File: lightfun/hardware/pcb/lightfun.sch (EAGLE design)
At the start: 10 parts, among them J1 FIRMWARE, P1 ESP8266, P2 ESP8266 CONNECTOR, P3 +5V GND, P4 TX RX, P5 GND, P6 +5V GND IO0 IO2, T1 LM2937ET

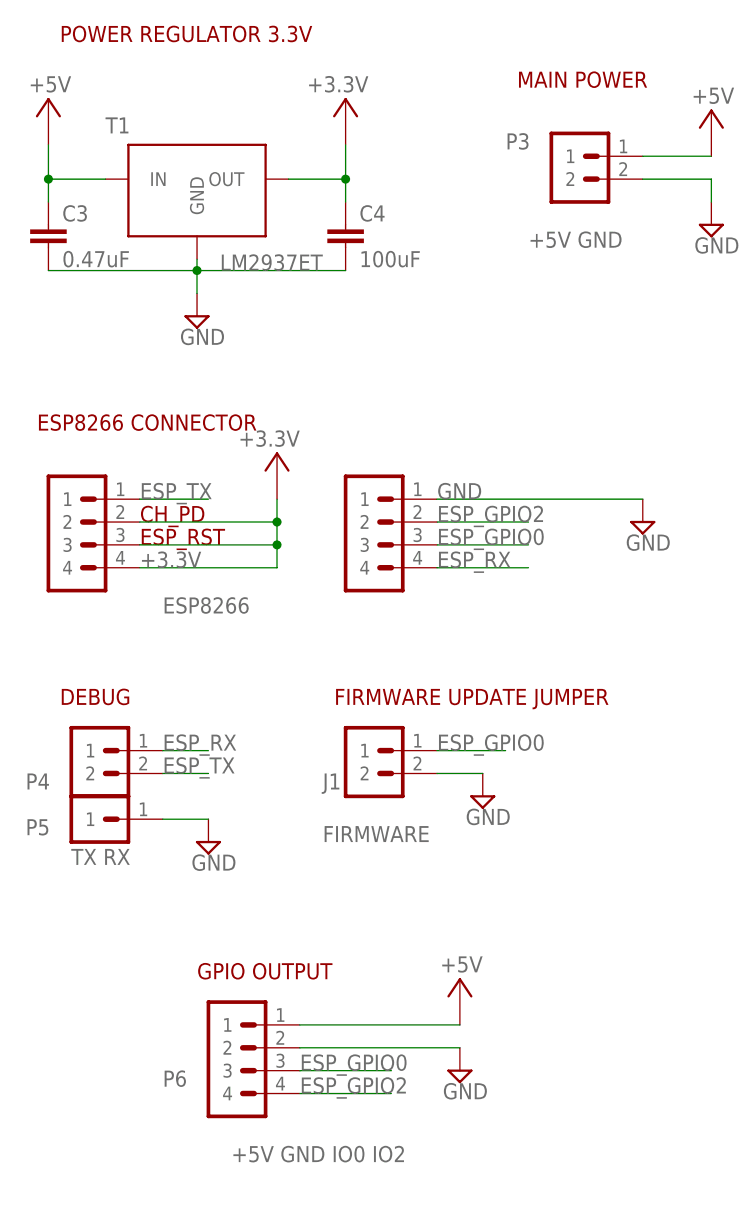
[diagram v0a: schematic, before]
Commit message: Generic ESP8266 PCB routing
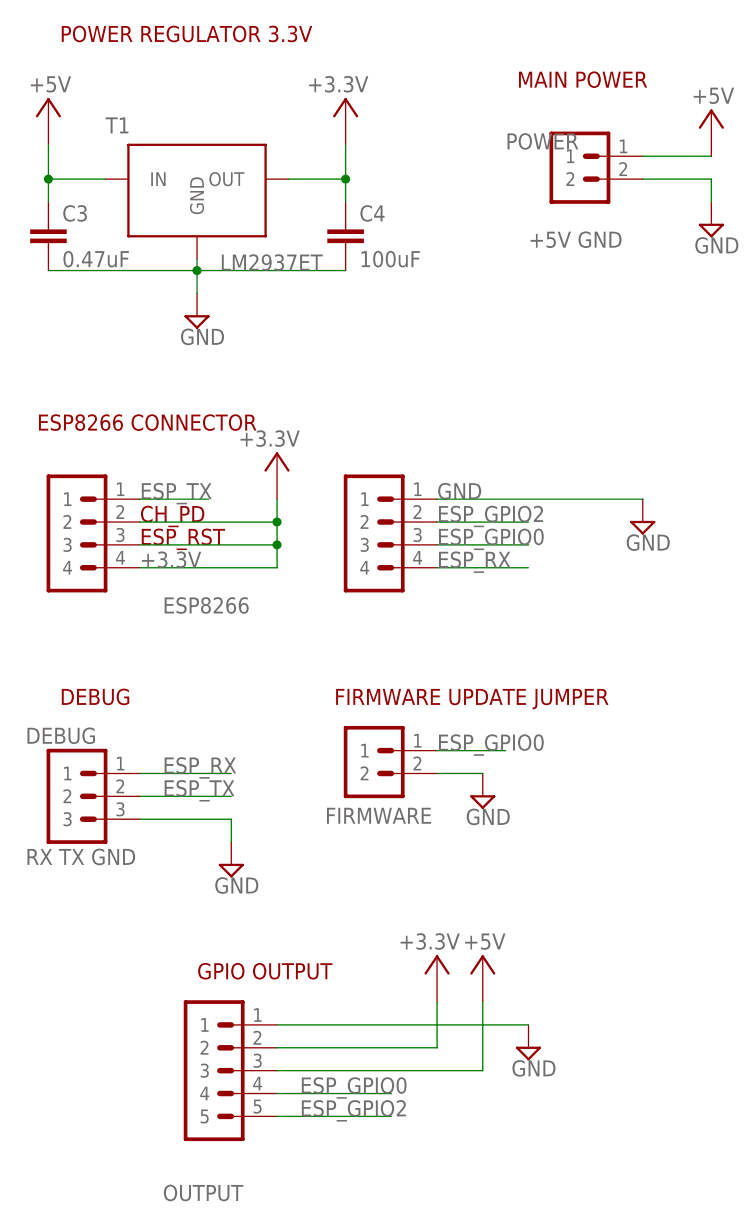
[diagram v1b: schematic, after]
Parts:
- removed P4: TX RX, stutz-eagle:PIN-HEADER-2PIN
- removed P5: GND, stutz-eagle:PIN-HEADER-1PIN
- removed P6: +5V GND IO0 IO2, stutz-eagle:PIN-HEADER-4PIN
- added DEBUG: RX TX GND, stutz-eagle:PIN-HEADER-3PIN
- added OUTPUT: GND 3.3V 5V IO0 IO2, stutz-eagle:PIN-HEADER-5PIN
- renumbered J1 to FIRMWARE, P3 to POWER
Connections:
- net +3.3V: now also OUTPUT.2
- net +5V: now also OUTPUT.3; no longer P6.1
- net ESP_GPIO0: now also OUTPUT.4; no longer P6.3
- net ESP_GPIO2: now also OUTPUT.5; no longer P6.4
- net ESP_RX: now also DEBUG.1; no longer P4.1
- net ESP_TX: now also DEBUG.2; no longer P4.2
- net GND: now also DEBUG.3, OUTPUT.1; no longer P5.1, P6.2
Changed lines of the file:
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@@
 <setting verticaltext="up"/>
 </settings>
-<grid distance="0.1" unitdist="inch" unit="inch" style="lines" multiple="1" display="yes" altdistance="0.01" altunitdist="inch" altunit="inch"/>
+<grid distance="0.1" unitdist="inch" unit="inch" style="lines" multiple="1" display="no" altdistance="0.01" altunitdist="inch" altunit="inch"/>
 <layers>
 <layer number="1" name="Top" color="4" fill="1" visible="no" active="no"/>
@@
 <class number="2" name="comm-rs485" width="1.016" drill="0">
 </class>
-<class number="3" name="power-1A" width="0.4064" drill="0">
+<class number="3" name="power-2A" width="1.143" drill="0">
 </class>
 </classes>
@@
 <part name="P1" library="stutz-eagle" deviceset="PIN-HEADER-4PIN" device="" value="ESP8266"/>
 <part name="P2" library="stutz-eagle" deviceset="PIN-HEADER-4PIN" device="" value="ESP8266 CONNECTOR"/>
-<part name="P4" library="stutz-eagle" deviceset="PIN-HEADER-2PIN" device="" value="TX RX"/>
-<part name="P3" library="stutz-eagle" deviceset="PIN-HEADER-2PIN" device="" value="+5V GND"/>
+<part name="POWER" library="stutz-eagle" deviceset="PIN-HEADER-2PIN" device="" value="+5V GND"/>
 <part name="SUPPLY1" library="stutz-eagle" deviceset="+5V" device=""/>
 <part name="SUPPLY2" library="supply2" deviceset="GND" device=""/>
-<part name="P5" library="stutz-eagle" deviceset="PIN-HEADER-1PIN" device="" value="GND"/>
 <part name="SUPPLY4" library="supply2" deviceset="GND" device=""/>
 <part name="SUPPLY5" library="stutz-eagle" deviceset="+3.3V" device=""/>
 <part name="SUPPLY6" library="supply2" deviceset="GND" device=""/>
-<part name="J1" library="stutz-eagle" deviceset="PIN-HEADER-2PIN" device="" value="FIRMWARE"/>
+<part name="FIRMWARE" library="stutz-eagle" deviceset="PIN-HEADER-2PIN" device="" value="FIRMWARE"/>
 <part name="SUPPLY7" library="supply2" deviceset="GND" device=""/>
-<part name="P6" library="stutz-eagle" deviceset="PIN-HEADER-4PIN" device="" value="+5V GND IO0 IO2"/>
+<part name="OUTPUT" library="stutz-eagle" deviceset="PIN-HEADER-5PIN" device="" value="GND 3.3V 5V IO0 IO2"/>
 <part name="SUPPLY8" library="supply2" deviceset="GND" device=""/>
 <part name="SUPPLY9" library="stutz-eagle" deviceset="+5V" device=""/>
+<part name="DEBUG" library="stutz-eagle" deviceset="PIN-HEADER-3PIN" device="" value="RX TX GND"/>
+<part name="SUPPLY10" library="stutz-eagle" deviceset="+3.3V" device=""/>
 </parts>
 <sheets>
@@
 </instance>
 <instance part="P2" gate="G$1" x="53.34" y="109.22" smashed="yes"/>
-<instance part="P4" gate="G$1" x="22.86" y="83.82" smashed="yes">
-<attribute name="VALUE" x="17.78" y="73.66" size="1.778" layer="96"/>
-<attribute name="NAME" x="12.7" y="82.042" size="1.778" layer="95"/>
-</instance>
-<instance part="P3" gate="G$1" x="76.2" y="149.86" smashed="yes">
+<instance part="POWER" gate="G$1" x="76.2" y="149.86" smashed="yes">
 <attribute name="VALUE" x="68.58" y="142.24" size="1.778" layer="96"/>
 <attribute name="NAME" x="66.04" y="153.162" size="1.778" layer="95"/>
@@
 <instance part="SUPPLY1" gate="G$1" x="88.9" y="154.94"/>
 <instance part="SUPPLY2" gate="GND" x="88.9" y="144.78"/>
-<instance part="P5" gate="G$1" x="20.32" y="78.74" smashed="yes">
-<attribute name="NAME" x="12.7" y="76.962" size="1.778" layer="95"/>
-</instance>
-<instance part="SUPPLY4" gate="GND" x="33.02" y="76.2"/>
+<instance part="SUPPLY4" gate="GND" x="35.56" y="73.66"/>
 <instance part="SUPPLY5" gate="G$1" x="40.64" y="116.84"/>
 <instance part="SUPPLY6" gate="GND" x="81.28" y="111.76"/>
-<instance part="J1" gate="G$1" x="53.34" y="83.82" smashed="yes">
-<attribute name="VALUE" x="45.72" y="76.2" size="1.778" layer="96"/>
-<attribute name="NAME" x="45.72" y="82.042" size="1.778" layer="95"/>
+<instance part="FIRMWARE" gate="G$1" x="53.34" y="83.82" smashed="yes">
+<attribute name="NAME" x="45.974" y="78.232" size="1.778" layer="95"/>
 </instance>
 <instance part="SUPPLY7" gate="GND" x="63.5" y="81.28"/>
-<instance part="P6" gate="G$1" x="38.1" y="50.8" smashed="yes">
-<attribute name="VALUE" x="35.56" y="40.64" size="1.778" layer="96"/>
-<attribute name="NAME" x="27.94" y="49.022" size="1.778" layer="95"/>
-</instance>
-<instance part="SUPPLY8" gate="GND" x="60.96" y="50.8"/>
-<instance part="SUPPLY9" gate="G$1" x="60.96" y="58.42"/>
+<instance part="OUTPUT" gate="G$1" x="33.02" y="50.8" smashed="yes">
+<attribute name="NAME" x="27.94" y="36.322" size="1.778" layer="95"/>
+</instance>
+<instance part="SUPPLY8" gate="GND" x="68.58" y="53.34"/>
+<instance part="SUPPLY9" gate="G$1" x="63.5" y="60.96"/>
+<instance part="DEBUG" gate="G$1" x="17.78" y="81.28"/>
+<instance part="SUPPLY10" gate="G$1" x="58.42" y="60.96"/>
 </instances>
 <busses>
@@
 </segment>
 <segment>
-<pinref part="P3" gate="G$1" pin="2"/>
+<pinref part="POWER" gate="G$1" pin="2"/>
 <pinref part="SUPPLY2" gate="GND" pin="GND"/>
 <wire x1="81.28" y1="149.86" x2="88.9" y2="149.86" width="0.1524" layer="91"/>
@@
 </segment>
 <segment>
-<pinref part="P5" gate="G$1" pin="1"/>
 <pinref part="SUPPLY4" gate="GND" pin="GND"/>
-<wire x1="27.94" y1="78.74" x2="33.02" y2="78.74" width="0.1524" layer="91"/>
-</segment>
-<segment>
-<pinref part="J1" gate="G$1" pin="2"/>
+<pinref part="DEBUG" gate="G$1" pin="3"/>
+<wire x1="25.4" y1="78.74" x2="35.56" y2="78.74" width="0.1524" layer="91"/>
+<wire x1="35.56" y1="78.74" x2="35.56" y2="76.2" width="0.1524" layer="91"/>
+</segment>
+<segment>
+<pinref part="FIRMWARE" gate="G$1" pin="2"/>
 <pinref part="SUPPLY7" gate="GND" pin="GND"/>
 <wire x1="58.42" y1="83.82" x2="63.5" y2="83.82" width="0.1524" layer="91"/>
 </segment>
 <segment>
-<pinref part="P6" gate="G$1" pin="2"/>
-<wire x1="43.18" y1="53.34" x2="60.96" y2="53.34" width="0.1524" layer="91"/>
+<pinref part="OUTPUT" gate="G$1" pin="1"/>
 <pinref part="SUPPLY8" gate="GND" pin="GND"/>
+<wire x1="40.64" y1="55.88" x2="68.58" y2="55.88" width="0.1524" layer="91"/>
 </segment>
 </net>
@@
 <junction x="40.64" y="109.22"/>
 </segment>
+<segment>
+<pinref part="OUTPUT" gate="G$1" pin="2"/>
+<pinref part="SUPPLY10" gate="G$1" pin="+3.3V"/>
+<wire x1="40.64" y1="53.34" x2="58.42" y2="53.34" width="0.1524" layer="91"/>
+<wire x1="58.42" y1="53.34" x2="58.42" y2="58.42" width="0.1524" layer="91"/>
+</segment>
 </net>
 <net name="+5V" class="3">
@@
 </segment>
 <segment>
-<pinref part="P3" gate="G$1" pin="1"/>
+<pinref part="POWER" gate="G$1" pin="1"/>
 <pinref part="SUPPLY1" gate="G$1" pin="+5V"/>
 <wire x1="81.28" y1="152.4" x2="88.9" y2="152.4" width="0.1524" layer="91"/>
 </segment>
 <segment>
-<pinref part="P6" gate="G$1" pin="1"/>
-<wire x1="43.18" y1="55.88" x2="60.96" y2="55.88" width="0.1524" layer="91"/>
+<pinref part="OUTPUT" gate="G$1" pin="3"/>
 <pinref part="SUPPLY9" gate="G$1" pin="+5V"/>
+<wire x1="40.64" y1="50.8" x2="63.5" y2="50.8" width="0.1524" layer="91"/>
+<wire x1="63.5" y1="50.8" x2="63.5" y2="58.42" width="0.1524" layer="91"/>
 </segment>
 </net>
@@
 </segment>
 <segment>
-<pinref part="P4" gate="G$1" pin="2"/>
-<wire x1="27.94" y1="83.82" x2="33.02" y2="83.82" width="0.1524" layer="91"/>
-<label x="27.94" y="83.82" size="1.778" layer="95"/>
+<wire x1="35.56" y1="81.28" x2="25.4" y2="81.28" width="0.1524" layer="91"/>
+<label x="27.94" y="81.28" size="1.778" layer="95"/>
+<pinref part="DEBUG" gate="G$1" pin="2"/>
 </segment>
 </net>
@@
 </segment>
 <segment>
-<pinref part="P6" gate="G$1" pin="4"/>
-<wire x1="43.18" y1="48.26" x2="53.34" y2="48.26" width="0.1524" layer="91"/>
-<label x="43.18" y="48.26" size="1.778" layer="95"/>
+<pinref part="OUTPUT" gate="G$1" pin="5"/>
+<wire x1="40.64" y1="45.72" x2="53.34" y2="45.72" width="0.1524" layer="91"/>
+<label x="43.18" y="45.72" size="1.778" layer="95"/>
 </segment>
 </net>
@@
 </segment>
 <segment>
-<pinref part="J1" gate="G$1" pin="1"/>
+<pinref part="FIRMWARE" gate="G$1" pin="1"/>
 <wire x1="58.42" y1="86.36" x2="66.04" y2="86.36" width="0.1524" layer="91"/>
 <label x="58.42" y="86.36" size="1.778" layer="95"/>
 </segment>
 <segment>
-<pinref part="P6" gate="G$1" pin="3"/>
-<wire x1="43.18" y1="50.8" x2="53.34" y2="50.8" width="0.1524" layer="91"/>
-<label x="43.18" y="50.8" size="1.778" layer="95"/>
+<pinref part="OUTPUT" gate="G$1" pin="4"/>
+<wire x1="40.64" y1="48.26" x2="53.34" y2="48.26" width="0.1524" layer="91"/>
+<label x="43.18" y="48.26" size="1.778" layer="95"/>
 </segment>
 </net>
@@
 </segment>
 <segment>
-<pinref part="P4" gate="G$1" pin="1"/>
-<wire x1="27.94" y1="86.36" x2="33.02" y2="86.36" width="0.1524" layer="91"/>
-<label x="27.94" y="86.36" size="1.778" layer="95"/>
-</segment>
-</net>
+<wire x1="35.56" y1="83.82" x2="25.4" y2="83.82" width="0.1524" layer="91"/>
+<label x="27.94" y="83.82" size="1.778" layer="95"/>
+<pinref part="DEBUG" gate="G$1" pin="1"/>
+</segment>
+</net>

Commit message: PCB update
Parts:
- removed DEBUG: RX TX GND, stutz-eagle:PIN-HEADER-3PIN
- removed POWER: +5V GND, stutz-eagle:PIN-HEADER-2PIN
- added C1, C7: 0.1uF, capacitor-wima:C2.5/2
- added C2, C5: 10uF, capacitor-wima:C2.5/2
- added C6: 0.22uF, capacitor-wima:C2.5/2
- added POWER_IN: GND +5V <35V, stutz-eagle:PIN-HEADER-3PIN
- added T2: LM7805, stutz-eagle:LM7805
- added UART: 3.3V RX TX GND, stutz-eagle:PIN-HEADER-4PIN
- C3: value 0.47uF -> 470uF
- C4: value 100uF -> 470uF
- T1: value LM2937ET -> AMS1117; device stutz-eagle:LM2937ET -> stutz-eagle:AMS1117
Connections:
- new net +24V: C6.1, POWER_IN.3, T2.IN
- net +3.3V: now also C1.1, C5.1, UART.1
- net +5V: now also C2.1, C7.1, POWER_IN.2, T2.OUT; no longer POWER.1
- net ESP_RX: now also UART.2; no longer DEBUG.1
- net ESP_TX: now also UART.3; no longer DEBUG.2
- net GND: now also C1.2, C2.2, C5.2, C6.2, C7.2, POWER_IN.1, T2.GND, UART.4; no longer DEBUG.3, POWER.2
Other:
- note added: "POWER REGULATOR 5V OPTIONAL FOR 8-35V INPUTS"
- moved on the sheet: FIRMWARE, OUTPUT
